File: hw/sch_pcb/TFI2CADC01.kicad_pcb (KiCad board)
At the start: 2 copper layers, 25 x 15 mm, 19 parts, among them J1 HEADER_2x04, J2 SM04B-GHS-TB, J3 SM04B-GHS-TB, T1 ALERT/RDY, U1 MIC5504-3.3YM5, U2 ADS1115IDGS

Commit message: Improve layout.
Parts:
- D3: moved to F.Cu
- moved R4 4.66 mm to (147.4, 109.4), turned to 0 degrees
- moved D3 1.01 mm to (142.9, 109.4), turned to 0 degrees
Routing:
- net +3V3: track 27.4 -> 21.5 mm
- net +5V: track 23.2 -> 21.3 mm
- net Net-(D3-A): track 3.51 -> 2.79 mm, vias 1 -> 0
- net /ALERT/RDY: track 18.5 -> 18.9 mm, vias 2 -> 1

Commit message: Updating pcb
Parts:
- moved D3 0.15 mm to (143.0, 109.5)
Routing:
- net /ALERT/RDY: track 18.9 -> 5.55 mm
- net Net-(D3-A): track 2.79 -> 0.00 mm
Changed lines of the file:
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@@
 	(footprint "Mlab_D:LED_0805"
 		(layer "F.Cu")
-		(at 142.858 109.4012)
+		(at 143 109.45)
 		(property "Reference" "D3"
 			(at -1.016 -1.384299 180)
@@
 	)
 	(segment
-		(start 146.591699 109.4266)
-		(end 144.9759 109.4266)
-		(width 0.3)
-		(layer "F.Cu")
-		(net 6)
-	)
-	(segment
-		(start 144.9505 109.4012)
-		(end 143.8105 109.4012)
-		(width 0.3)
-		(layer "F.Cu")
-		(net 6)
-	)
-	(segment
-		(start 144.9759 109.4266)
-		(end 144.9505 109.4012)
-		(width 0.3)
-		(layer "F.Cu")
-		(net 6)
-	)
-	(segment
 		(start 153.2926 105.215)
 		(end 154.0594 104.4482)
@@
 	)
 	(segment
-		(start 143.0104 110.7728)
-		(end 146.5664 110.7728)
-		(width 0.3)
-		(layer "F.Cu")
-		(net 11)
-	)
-	(segment
-		(start 142.3514 109.8471)
-		(end 142.3514 110.1138)
-		(width 0.3)
-		(layer "F.Cu")
-		(net 11)
-	)
-	(segment
 		(start 155.38 106.628)
 		(end 155.38 109.19)
@@
 	)
 	(segment
-		(start 147.049 110.2902)
-		(end 154.2798 110.2902)
-		(width 0.3)
-		(layer "F.Cu")
-		(net 11)
-	)
-	(segment
-		(start 146.5664 110.7728)
-		(end 147.049 110.2902)
-		(width 0.3)
-		(layer "F.Cu")
-		(net 11)
-	)
-	(segment
 		(start 154.2798 110.2902)
 		(end 155.38 109.19)
 		(width 0.3)
 		(layer "F.Cu")
-		(net 11)
-	)
-	(segment
-		(start 142.3514 110.1138)
-		(end 143.0104 110.7728)
-		(width 0.3)
-		(layer "F.Cu")
-		(net 11)
-	)
-	(segment
-		(start 141.9055 109.4012)
-		(end 142.3514 109.8471)
-		(width 0.3)
-		(layer "F.Cu")

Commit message: Updating pcb
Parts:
- D1: moved to F.Cu
- moved R4 1.33 mm to (146.1, 109.4)
- moved D1 1.05 mm to (142.8, 100.4)
- moved R1 0.38 mm to (143.3, 102.8)
- moved D3 0.20 mm to (142.8, 109.5)
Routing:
- net /ALERT/RDY: track 5.55 -> 19.5 mm
- net Net-(D3-A): track 0.00 -> 1.52 mm
- net Net-(D1-A): track 3.99 -> 2.83 mm, vias 1 -> 0
- net +3V3: track 21.5 -> 22.4 mm
- net GND: vias 18 -> 17
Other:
- board text removed: "K"

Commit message: Improve silkscreen.
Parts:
- added G***: LOGO, TF_LOGA:TF 10x4,7, B.Cu at (146.9, 109.7)
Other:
- board text added: "TFI2CADC01A"

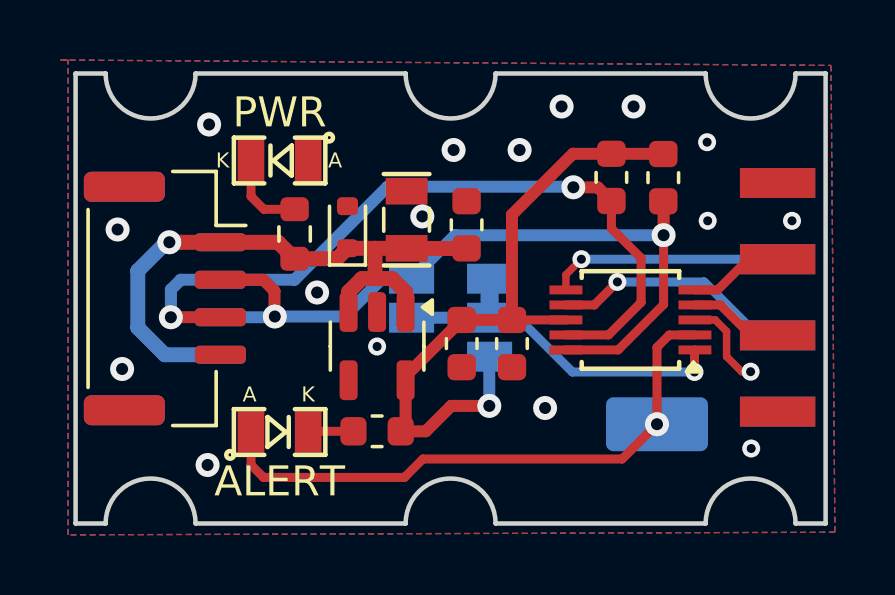
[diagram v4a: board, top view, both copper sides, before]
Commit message: Improve layout. Fix DRC and ERC errors. Improve PinHeader edge-mount footprint. Update footprints.
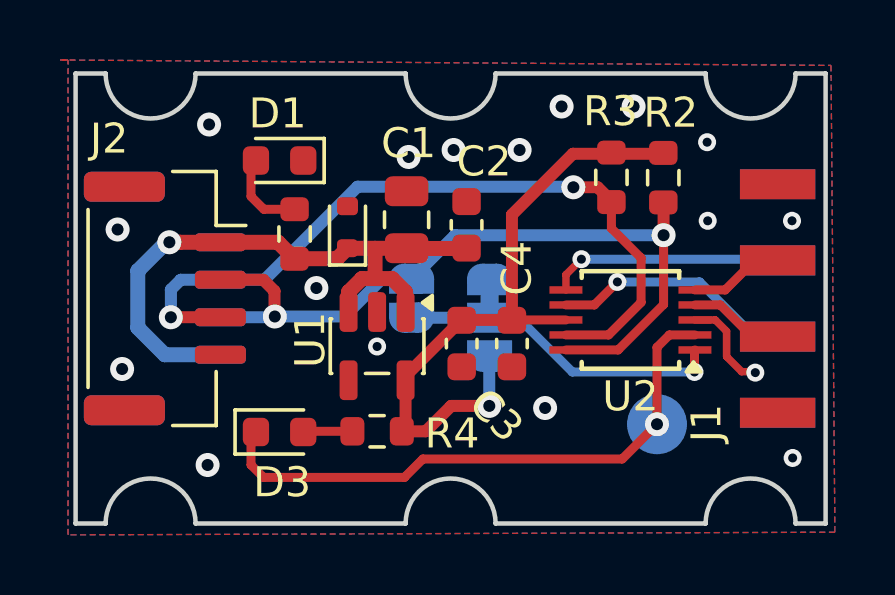
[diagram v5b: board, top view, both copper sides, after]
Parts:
- C1: footprint Mlab_R:SMD-0805 -> Capacitor_SMD:C_0805_2012Metric
- C2, C3, C4: footprint Mlab_R:SMD-0603 -> Capacitor_SMD:C_0603_1608Metric
- D1, D3: footprint Mlab_D:LED_0805 -> LED_SMD:LED_0603_1608Metric
- J1: footprint Connector_PinHeader_2.54mm:PinHeader_2x04_P2.54mm_Edge_Mount -> Mlab_Pin_Headers:PinHeader_2x04_P2.54mm_Edge_Mount
- JP1: footprint Jumper:SolderJumper-3_P1.3mm_Bridged12_Pad1.0x1.5mm_NumberLabels -> Jumper:SolderJumper-3_P1.3mm_Bridged12_RoundedPad1.0x1.5mm
- JP2: footprint Jumper:SolderJumper-2_P1.3mm_Open_Pad1.0x1.5mm -> Jumper:SolderJumper-2_P1.3mm_Open_RoundedPad1.0x1.5mm
- R2, R3, R4: footprint Mlab_R:SMD-0603 -> Resistor_SMD:R_0603_1608Metric
- T1: footprint TestPoint:TestPoint_Keystone_5015_Micro_Mini -> TestPoint:TestPoint_Pad_D2.0mm
- moved J1 0.25 mm to (159.4, 105.0)
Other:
- rule pad_to_mask_clearance: 0.2 -> 0.05

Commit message: Improve footprint selection. Fix layout Documentation update.
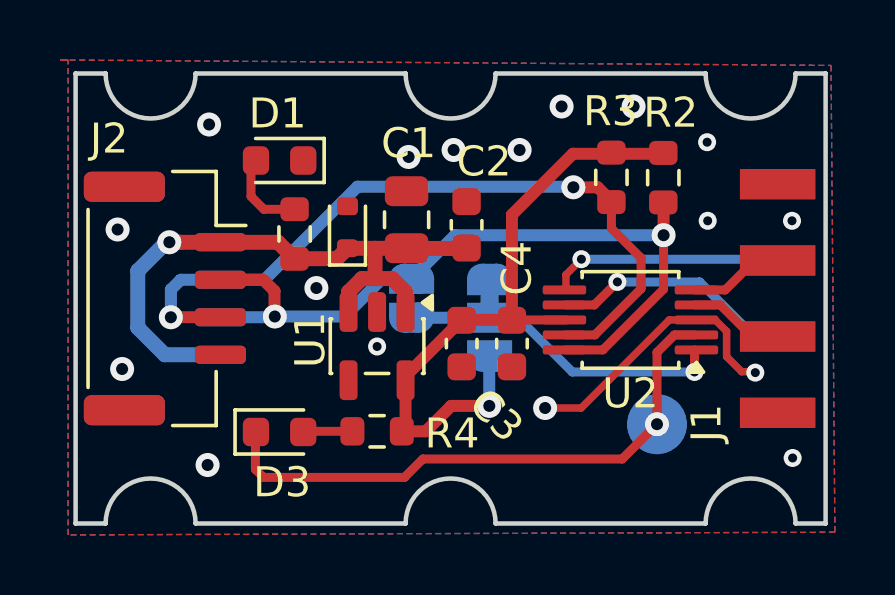
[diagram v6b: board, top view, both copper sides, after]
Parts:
- U2: footprint Package_SO:TSSOP-10_3x3mm_P0.5mm -> Package_SO:VSSOP-10_3x3mm_P0.5mm
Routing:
- net GND: track 3.82 -> 10.0 mm
